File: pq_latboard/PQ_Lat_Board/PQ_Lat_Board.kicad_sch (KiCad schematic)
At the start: 12 parts, among them IC1 TCN75AVUA713-VAO, J1 Conn_01x11_MountingPin

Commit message: lots of changes
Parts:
- removed R1, R2: 5k, Resistor_SMD:R_0805_2012Metric, symbol Lateral_board-altium-import:0_5k
- added C1: 100 nF, Capacitor_SMD:C_0603_1608Metric, symbol Device:C
- added H1, H2, H3, H4: MountingHole_Pad, MountingHole:MountingHole_2.2mm_M2_Pad, symbol Mechanical:MountingHole_Pad
- D1: footprint (none) -> GGS_Miscellaneous:SLCD-61N8
- GA0, GA1, GA2, VA0, VA1, VA2: value 5k -> 0R
- IC1: value TCN75AVUA713-VAO -> TCN75AVOA713
- J1: footprint (none) -> Connector_Molex:Molex_PicoBlade_53261-1071_1x10-1MP_P1.25mm_Horizontal
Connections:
- net ADCS_GND is gone; now on net ADCS: J1.2 (Pin_2)
- net ADCS: no longer J1.3 (Pin_3)
- net GND: now also C1.2, H1.1, H2.1, H3.1, H4.1
- net VCC: now also C1.1
- net Pout renamed SOLAR
- new net VCC_MAG: J1.3 (Pin_3)

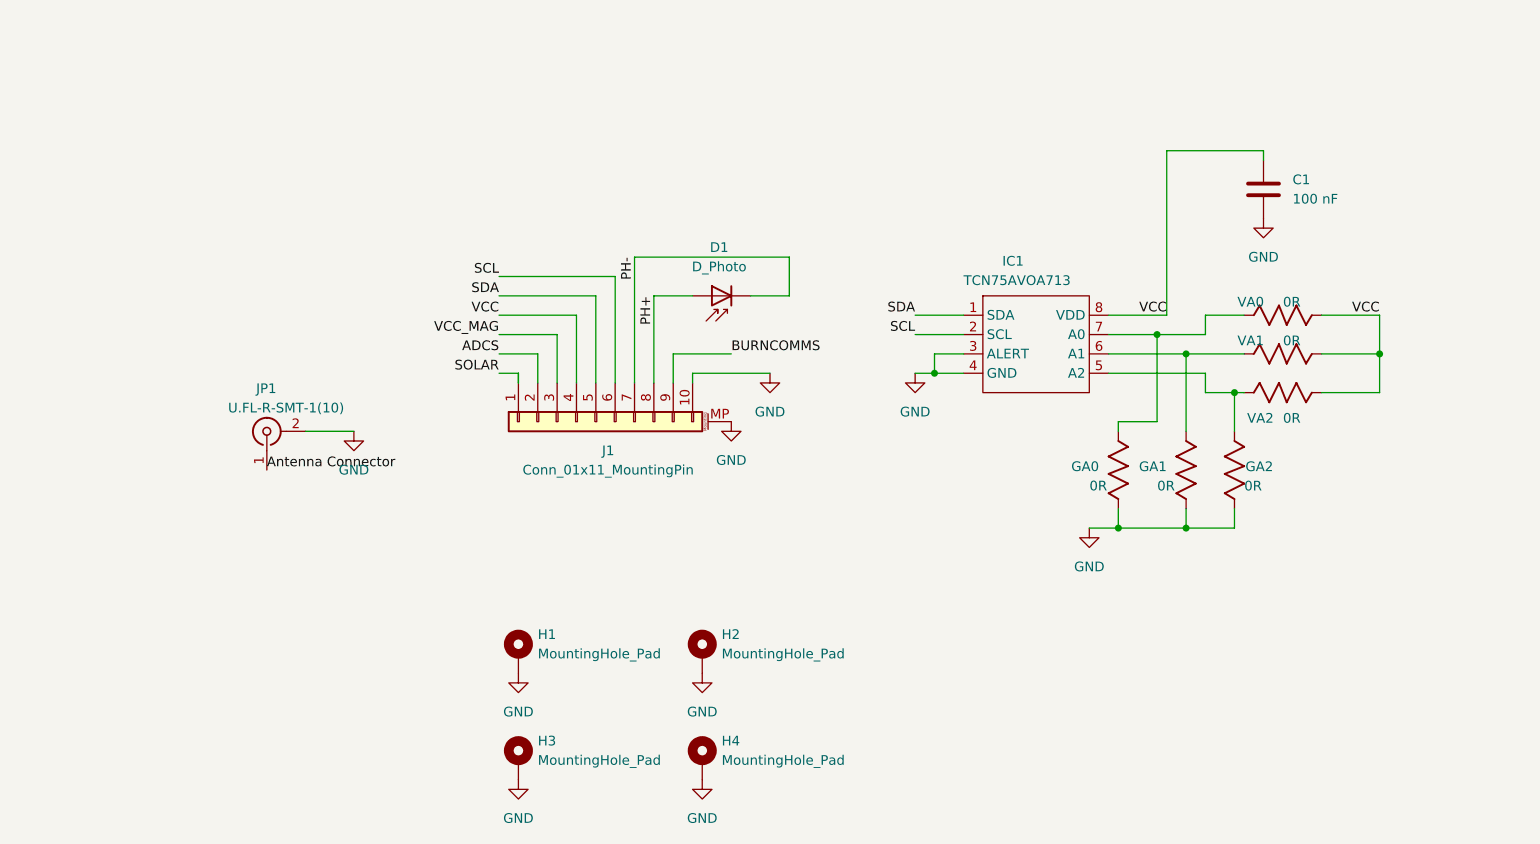
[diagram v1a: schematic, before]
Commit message: Lateral, Bottom and MagY boards done
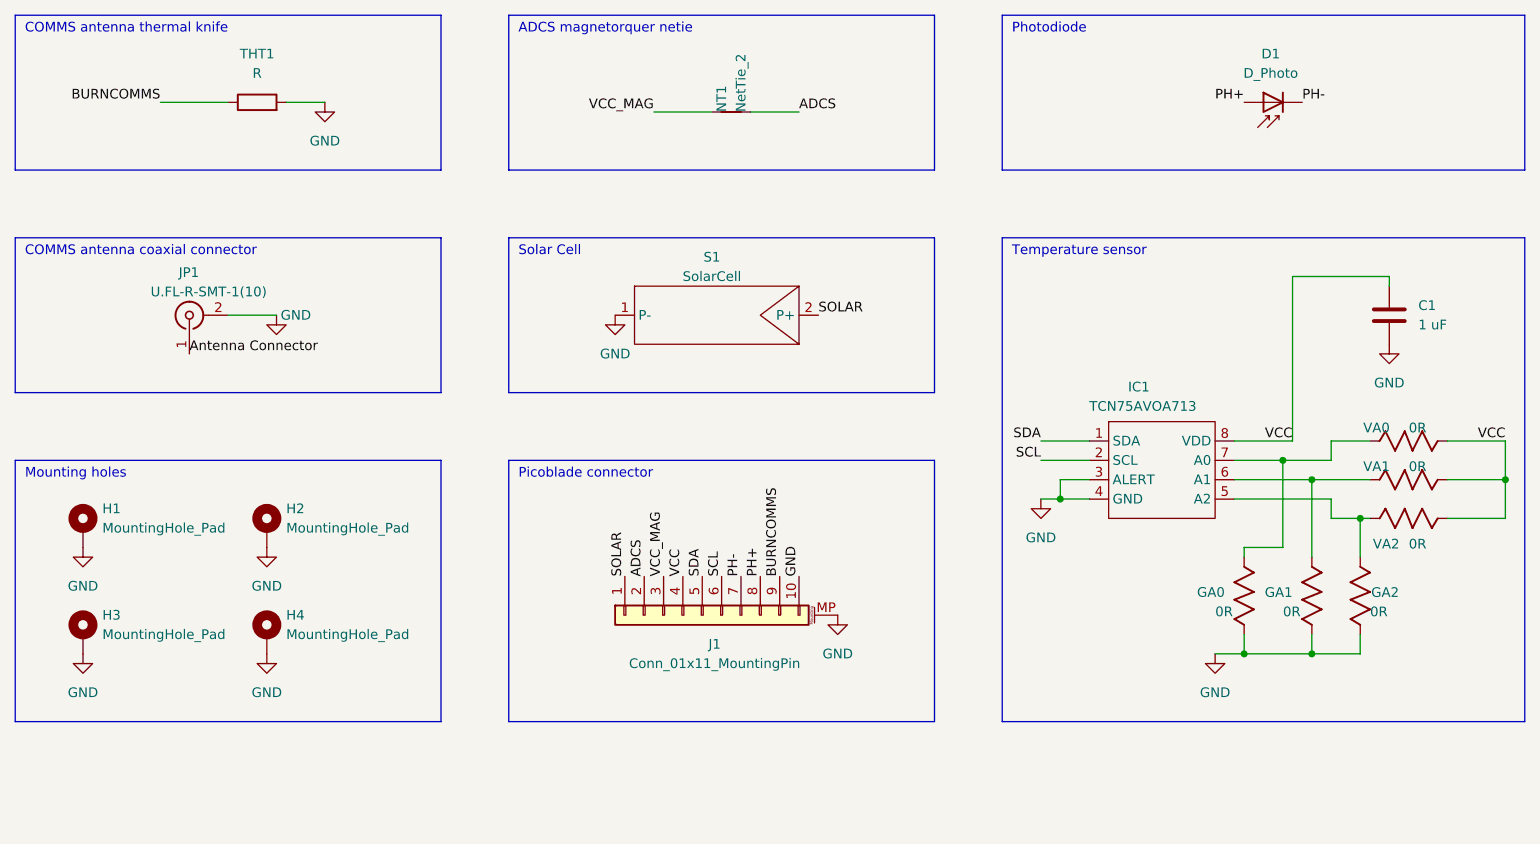
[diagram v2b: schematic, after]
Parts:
- added NT1: NetTie_2, NetTie:NetTie-2_SMD_Pad0.5mm, symbol Device:NetTie_2
- added S1: SolarCell, NSL_power:Solar_Cell, symbol NSL_power:SolarCell
- added THT1: R, Resistor_THT:R_Axial_DIN0309_L9.0mm_D3.2mm_P12.70mm_Horizontal, symbol Device:R
- C1: value 100 nF -> 1 uF
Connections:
- net ADCS: now also NT1.2
- net BURNCOMMS: now also THT1.1
- net GND: now also S1.1 (P-), THT1.2
- net SOLAR: now also S1.2 (P+)
- net VCC_MAG: now also NT1.1
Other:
- note added: "ADCS magnetorquer netie"
- note added: "COMMS antenna coaxial connector"
- note added: "COMMS antenna thermal knife"
- note added: "Mounting holes"
- note added: "Photodiode"
- note added: "Picoblade connector"
- note added: "Solar Cell"
- note added: "Temperature sensor"
- moved on the sheet: C1, D1, GA0, GA1, GA2, H1, H2, H3, H4, IC1, J1, JP1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

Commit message: Functional revision and finishing touches part I
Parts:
- removed D1: D_Photo, GGS_Miscellaneous:SLCD-61N8, symbol Device:D_Photo
- removed JP1: U.FL-R-SMT-1(10), Connector_Coaxial:U.FL_Hirose_U.FL-R-SMT-1_Vertical, symbol Connector:Conn_Coaxial
- removed S1: SolarCell, NSL_power:Solar_Cell, symbol NSL_power:SolarCell
- added D1: SLCD-61N8, passive-nsl:SLCD-61N8, symbol passive-nsl:SLCD-61N8
- added H5: MountingHole_Pad, MountingHole:MountingHole_2.2mm_M2_DIN965_Pad_TopOnly, symbol Mechanical:MountingHole_Pad
- added J2: connector-coax, connector-nsl:C.FL-R-SMT-1(90), symbol connector-nsl:connector-coax
- added SC1: Solar_Cell, power-nsl:Azur-Space-PQ-cut-SC, symbol power-nsl:Solar_Cell
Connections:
- net Antenna Connector: now also H5.1, J2.1
- net GND: now also J2.2, SC1.1 (-)
- net PH+: now also D1.2
- net PH-: now also D1.1
- net SOLAR: now also SC1.2

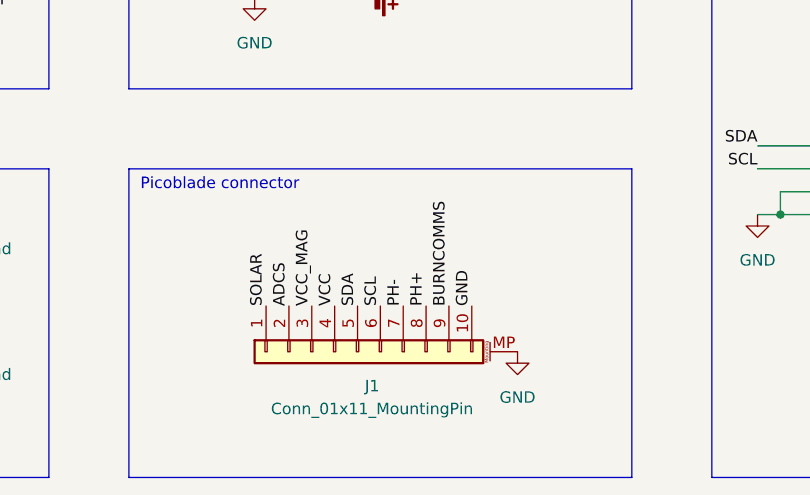
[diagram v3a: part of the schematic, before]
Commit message: Full Kicad7 transition, library improvement and adaptation, correct footprints and 3D models added
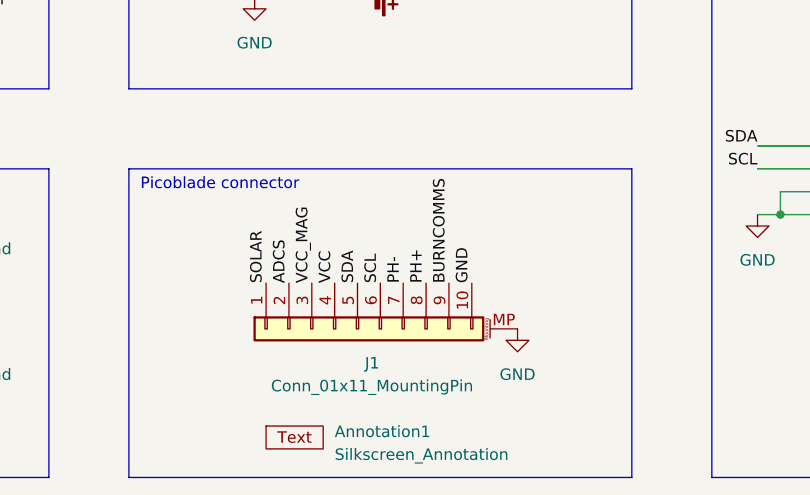
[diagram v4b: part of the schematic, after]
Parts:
- added Annotation1: Silkscreen_Annotation, -nsl_symbols:Bridgemaker, symbol -nsl_symbols:Silkscreen_Annotation
- D1: footprint passive-nsl:SLCD-61N8 -> -nsl_passive:SLCD-61N8
- IC1: footprint Package_SO:SOP-8_3.9x4.9mm_P1.27mm -> -nsl_sensor:TCN75AVOA
- J2: footprint connector-nsl:C.FL-R-SMT-1(90) -> -nsl_connector:C.FL-R-SMT-1(90)
- SC1: footprint power-nsl:Azur-Space-PQ-cut-SC -> -nsl_power:Azur-Space-PQ-cut-SC
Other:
- moved on the sheet: J1

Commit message: Small changes of component fields for the BOM
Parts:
- GA0, GA1, GA2, VA0, VA1, VA2: Manufacturer 1 (none) -> Vishay / Dale; Manufacturer Part Number 1 (none) -> CRCW08055K00JNTA; Supplier 1 (none) -> Mouser; Supplier Part Number 1 (none) -> 71-CRCW0805J-5K
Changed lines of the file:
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@@
       (effects (font (size 1.27 1.27)) (justify left bottom) hide)
+    )
+    (property "Manufacturer 1" "Vishay / Dale" (at 210.82 129.54 0)
+      (effects (font (size 1.27 1.27)) hide)
+    )
+    (property "Manufacturer Part Number 1" "CRCW08055K00JNTA" (at 210.82 129.54 0)
+      (effects (font (size 1.27 1.27)) hide)
+    )
+    (property "Supplier 1" "Mouser" (at 210.82 129.54 0)
+      (effects (font (size 1.27 1.27)) hide)
+    )
+    (property "Supplier Part Number 1" "71-CRCW0805J-5K" (at 210.82 129.54 0)
+      (effects (font (size 1.27 1.27)) hide)
     )
     (pin "1")
@@
     (property "BOM_LINK" "https://www.mouser.es/ProductDetail/Vishay-Dale/CRCW08055K00JNTA?qs=%2Fha2pyFadui6t5gBae62ocFJ46SNue422n5luvT1xmc7fnXInubqKA%3D%3D" (at 219.71 129.54 0)
       (effects (font (size 1.27 1.27)) (justify left bottom) hide)
+    )
+    (property "Manufacturer 1" "Vishay / Dale" (at 219.71 129.54 0)
+      (effects (font (size 1.27 1.27)) hide)
+    )
+    (property "Manufacturer Part Number 1" "CRCW08055K00JNTA" (at 219.71 129.54 0)
+      (effects (font (size 1.27 1.27)) hide)
+    )
+    (property "Supplier 1" "Mouser" (at 219.71 129.54 0)
+      (effects (font (size 1.27 1.27)) hide)
+    )
+    (property "Supplier Part Number 1" "71-CRCW0805J-5K" (at 219.71 129.54 0)
+      (effects (font (size 1.27 1.27)) hide)
     )
     (pin "1")
@@
       (effects (font (size 1.27 1.27)) (justify left bottom) hide)
     )
+    (property "Manufacturer 1" "Vishay / Dale" (at 232.41 109.22 0)
+      (effects (font (size 1.27 1.27)) hide)
+    )
+    (property "Manufacturer Part Number 1" "CRCW08055K00JNTA" (at 232.41 109.22 0)
+      (effects (font (size 1.27 1.27)) hide)
+    )
+    (property "Supplier 1" "Mouser" (at 232.41 109.22 0)
+      (effects (font (size 1.27 1.27)) hide)
+    )
+    (property "Supplier Part Number 1" "71-CRCW0805J-5K" (at 232.41 109.22 0)
+      (effects (font (size 1.27 1.27)) hide)
+    )
     (pin "1")
     (pin "2")
@@
       (effects (font (size 1.27 1.27)) (justify left bottom) hide)
     )
+    (property "Manufacturer 1" "Vishay / Dale" (at 232.41 114.3 0)
+      (effects (font (size 1.27 1.27)) hide)
+    )
+    (property "Manufacturer Part Number 1" "CRCW08055K00JNTA" (at 232.41 114.3 0)
+      (effects (font (size 1.27 1.27)) hide)
+    )
+    (property "Supplier 1" "Mouser" (at 232.41 114.3 0)
+      (effects (font (size 1.27 1.27)) hide)
+    )
+    (property "Supplier Part Number 1" "71-CRCW0805J-5K" (at 232.41 114.3 0)
+      (effects (font (size 1.27 1.27)) hide)
+    )
     (pin "1")
     (pin "2")
@@
       (effects (font (size 1.27 1.27)) (justify left bottom) hide)
     )
+    (property "Manufacturer 1" "Vishay / Dale" (at 232.41 119.38 0)
+      (effects (font (size 1.27 1.27)) hide)
+    )
+    (property "Manufacturer Part Number 1" "CRCW08055K00JNTA" (at 232.41 119.38 0)
+      (effects (font (size 1.27 1.27)) hide)
+    )
+    (property "Supplier 1" "Mouser" (at 232.41 119.38 0)
+      (effects (font (size 1.27 1.27)) hide)
+    )
+    (property "Supplier Part Number 1" "71-CRCW0805J-5K" (at 232.41 119.38 0)
+      (effects (font (size 1.27 1.27)) hide)
+    )
     (pin "1")
     (pin "2")
@@
       (effects (font (size 1.27 1.27)) (justify left bottom) hide)
     )
-    (pin "1")
+    (property "Manufacturer 1" "Vishay / Dale" (at 226.06 129.54 0)
+      (effects (font (size 1.27 1.27)) hide)
+    )
+    (property "Manufacturer Part Number 1" "CRCW08055K00JNTA" (at 226.06 129.54 0)
+      (effects (font (size 1.27 1.27)) hide)
+    )
+    (property "Supplier 1" "Mouser" (at 226.06 129.54 0)
+      (effects (font (size 1.27 1.27)) hide)
+    )
+    (property "Supplier Part Number 1" "71-CRCW0805J-5K" (at 226.06 129.54 0)
+      (effects (font (size 1.27 1.27)) hide)
+    )
+    (pin "1")
